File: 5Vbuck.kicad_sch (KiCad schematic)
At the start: 0 parts

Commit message: jobbing med 5V og 12V
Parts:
- added C_BST1, C_Vin1: 0.1u, symbol Device:C
- added C_C4: 4.7n, symbol Device:C
- added C_C5: 100p, symbol Device:C
- added C_C6: 1n, symbol Device:C
- added C_ss1: 12.5n, symbol Device:C
- added R_BST1, R_Vin1: 2.2, symbol Device:R
- added R_C3: 8.06k, symbol Device:R
- added R_C4, R_UV4: 100k, symbol Device:R
- added R_FB1: 52.5k, symbol Device:R
- added R_FB2: 10k, symbol Device:R
- added R_RT1: 24.9k, symbol Device:R
- added R_UV3: 9.31k, symbol Device:R
- added U3: LM5146RGYR, LM5146RGYR:IC_LM5146RGYR, symbol LM5146RGYR:LM5146RGYR
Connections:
- new net: C_C4.1, R_C3.1
- new net: C_C5.2, C_C6.1, R_C3.2, R_C4.2, R_FB2.1
- new net: C_Vin1.2, R_UV4.2, R_Vin1.1, U3.20 (VIN)
- new net: C_C4.2, C_C5.1
- new net: R_BST1.1, U3.17 (BST)
- new net: C_BST1.1, R_BST1.2
- new net: C_BST1.2, U3.19 (SW)
- new net: R_UV3.2, R_UV4.1, U3.1 (EN/UVLO)
- new net: C_ss1.2, U3.3 (SS/TRK)
- new net: U3.16 (NC), U3.9 (NC)
- new net: R_RT1.2, U3.2 (RT)
- new net: R_C4.1, R_FB1.2
- new net: C_C6.2, R_FB1.1
- new net 5VSYNC_In: U3.8 (SYNCIN)
- new net 5VSYNC_Out: U3.7 (SYNCOUT)
- new net 5V_PGOOD: U3.10 (PGOOD)
- new net 5V_Vin: R_Vin1.2
- new net EP: U3.15 (EP), U3.21 (EP)
- new net GND: C_Vin1.1, C_ss1.1, R_FB2.2, R_RT1.1, R_UV3.1, U3.11 (ILIM), U3.6 (AGND)
- no-connect marks 0 -> 1

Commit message: navn på alle komp i 5V
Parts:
- removed C_BST1, C_Vin1: 0.1u, symbol Device:C
- removed C_C4: 4.7n, symbol Device:C
- removed C_C5: 100p, symbol Device:C
- removed C_C6: 1n, symbol Device:C
- removed C_ss1: 12.5n, symbol Device:C
- removed R_BST1, R_Vin1: 2.2, symbol Device:R
- removed R_C3: 8.06k, symbol Device:R
- removed R_C4, R_UV4: 100k, symbol Device:R
- removed R_FB1: 52.5k, symbol Device:R
- removed R_FB2: 10k, symbol Device:R
- removed R_RT1: 24.9k, symbol Device:R
- removed R_UV3: 9.31k, symbol Device:R
- added C401, C404: 0.1u, symbol Device:C
- added C402: 2.2u, symbol Device:C
- added C403: 47nF, symbol Device:C
- added C405: 10p, symbol Device:C
- added C406: 4.7n, symbol Device:C
- added C407: 100p, symbol Device:C
- added C408: 1n, symbol Device:C
- added C409, C410, C411, C412, C413: 2.2 u, symbol Device:C
- added C414, C415, C416, C417, C418: 22u, symbol Device:C
- added L401: L, Package_SO:SSOP-16_3.9x4.9mm_P0.635mm, symbol Device:L
- added Q3, Q4: NMOS, Package_DFN_QFN:Nordic_AQFN-94-1EP_7x7mm_P0.4mm, symbol Simulation_SPICE:NMOS
- added R401: 9.31k, symbol Device:R
- added R402, R409: 100k, symbol Device:R
- added R403, R405: 2.2, symbol Device:R
- added R406: 24.9 k, symbol Device:R
- added R407: 619, symbol Device:R
- added R408: 8.06k, symbol Device:R
- added R410: 21k, symbol Device:R
- added R411: 1.5k, symbol Device:R
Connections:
- net GND: now also U3.12 (PGND), C401.1, C402.2, C403.1, C405.2, C413.2, C418.2, Q4.3 (S), R401.1, R406.1, R411.2; no longer U3.11 (ILIM)
- net at U3.20 (VIN): now also C401.2, R402.2, R403.1
- net at U3.17 (BST): now also R405.1
- net at U3.19 (SW): now also C404.2, L401.1, Q3.3 (S), Q4.1 (D), R407.2
- net at U3.1 (EN/UVLO): now also R401.2, R402.1
- net at U3.3 (SS/TRK): now also C403.2
- net at U3.13 (LO): now also Q4.2 (G)
- net at U3.14 (VCC): now also C402.1
- net at U3.18 (HO): now also Q3.2 (G)
- net at U3.2 (RT): now also R406.2
- net Comp: now reaches U3.4 (COMP)
- net Comp: now also C406.2, C407.1
- net FB: now reaches U3.5 (FB)
- net FB: now also C407.2, C408.1, R408.2, R409.2, R411.1
- net 5VSYNC_In renamed 12VSYNC_In
- net 5VSYNC_Out renamed 12VSYNC_Out
- net 5V_PGOOD renamed 12V_PGOOD
- new net: C411.2, C412.1
- new net: C412.2, C413.1
- new net: C409.2, C410.1
- new net: C416.2, C417.1
- new net: C417.2, C418.1
- new net: C405.1, R407.1, U3.11 (ILIM)
- new net: C414.2, C415.1
- new net: C404.1, R405.2
- new net: C408.2, R410.1
- new net: C406.1, R408.1
- new net: C415.2, C416.1
- new net: C410.2, C411.1
- new net 12VV_out: C414.1, L401.2, R409.1, R410.2
- new net 12V_Vin: C409.1, Q3.1 (D), R403.2

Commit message: endring av kondensatorer
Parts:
- added R411: 20k, symbol Device:R
- C403: value 47nF -> 12.5nF
- C405: value 10p -> 47p
- C406: value 4.7n -> 2.3n
- C407: value 100p -> 22p
- C408: value 1n -> 820p
- L401: value L -> 15u
- R401: value 9.31k -> 14.3k
- R402: value 100k -> 200k
- R406: renamed from R407; value 619 -> 134
- R407: renamed from R408; value 8.06k -> 35.7k
- R408: renamed from R409; value 100k -> 52.5k; Field5 R_C2 -> R_FB1
- R409: renamed from R410; value 21k -> 100k; Field5 R_FB1 -> R_C2
- R410: renamed from R411; value 1.5k -> 10k; Field5 R_FB1 -> R_FB2
- renumbered R405 to R404, R406 to R405
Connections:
- net 12VV_out is gone; now on net 5V_Vout: C414.1, L401.2, R408.1, R409.2
- net 12V_Vin is gone; now on net 5V_Vin: C409.1, Q3.1 (D), R403.2
- net GND: now also C409.2, C410.2, C411.2, C412.2, C414.2, C415.2, C416.2, C417.2
- net 5V_Vin: now reaches C412.1
- net 5V_Vin: now also C410.1, C411.1, C413.1; no longer C411.2
- net V_cc: now reaches C402.1, U3.14 (VCC)
- net V_cc: now also R411.1
- net 5V_Vout: now reaches C417.1
- net 5V_Vout: now also C415.1, C416.1, C418.1; no longer C416.2
- net at C405.1, R406.1, U3.11 (ILIM): now also R411.2
- net 12VSYNC_In renamed 5VSYNC_In
- net 12VSYNC_Out renamed 5VSYNC_Out
- net 12V_PGOOD renamed 5V_PGOOD
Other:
- moved on the sheet: C406, C407, C408, C409, C410, C411, C412, C413, C414, C415, C416, C417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

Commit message: komp til 5V
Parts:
- C405: value 47p -> 39p
- C406: value 2.3n -> 12n
- C407: value 22p -> 120p
- C408: value 820p -> 4.7n
- R401: value 14.3k -> 12.7k
- R406: value 134 -> 137
- R407: value 35.7k -> 6.8k
- R408: value 52.5k -> 10k
- R409: value 100k -> 350
- R410: value 10k -> 1.91k
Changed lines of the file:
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@@
 			)
 		)
-		(property "Value" "134"
+		(property "Value" "137"
 			(at 124.46 123.19 90)
 			(show_name no)
@@
 			)
 		)
-		(property "Value" "14.3k"
+		(property "Value" "12.7k"
 			(at 66.04 62.23 90)
 			(show_name no)
@@
 			)
 		)
-		(property "Value" "10k"
+		(property "Value" "1.91k"
 			(at 176.53 139.6999 0)
 			(show_name no)
@@
 			)
 		)
-		(property "Value" "22p"
+		(property "Value" "120p"
 			(at 163.83 133.858 90)
 			(show_name no)
@@
 			)
 		)
-		(property "Value" "820p"
+		(property "Value" "4.7n"
 			(at 186.69 121.9199 0)
 			(show_name no)
@@
 			)
 		)
-		(property "Value" "2.3n"
+		(property "Value" "12n"
 			(at 160.02 115.57 90)
 			(show_name no)
@@
 			)
 		)
-		(property "Value" "52.5k"
+		(property "Value" "10k"
 			(at 176.53 116.8399 0)
 			(show_name no)
@@
 			)
 		)
-		(property "Value" "35.7k"
+		(property "Value" "6.8k"
 			(at 167.64 116.84 90)
 			(show_name no)
@@
 			)
 		)
-		(property "Value" "47p"
+		(property "Value" "39p"
 			(at 120.65 133.3499 0)
 			(show_name no)
@@
 			)
 		)
-		(property "Value" "100k"
+		(property "Value" "350"
 			(at 185.42 114.2999 0)
 			(show_name no)

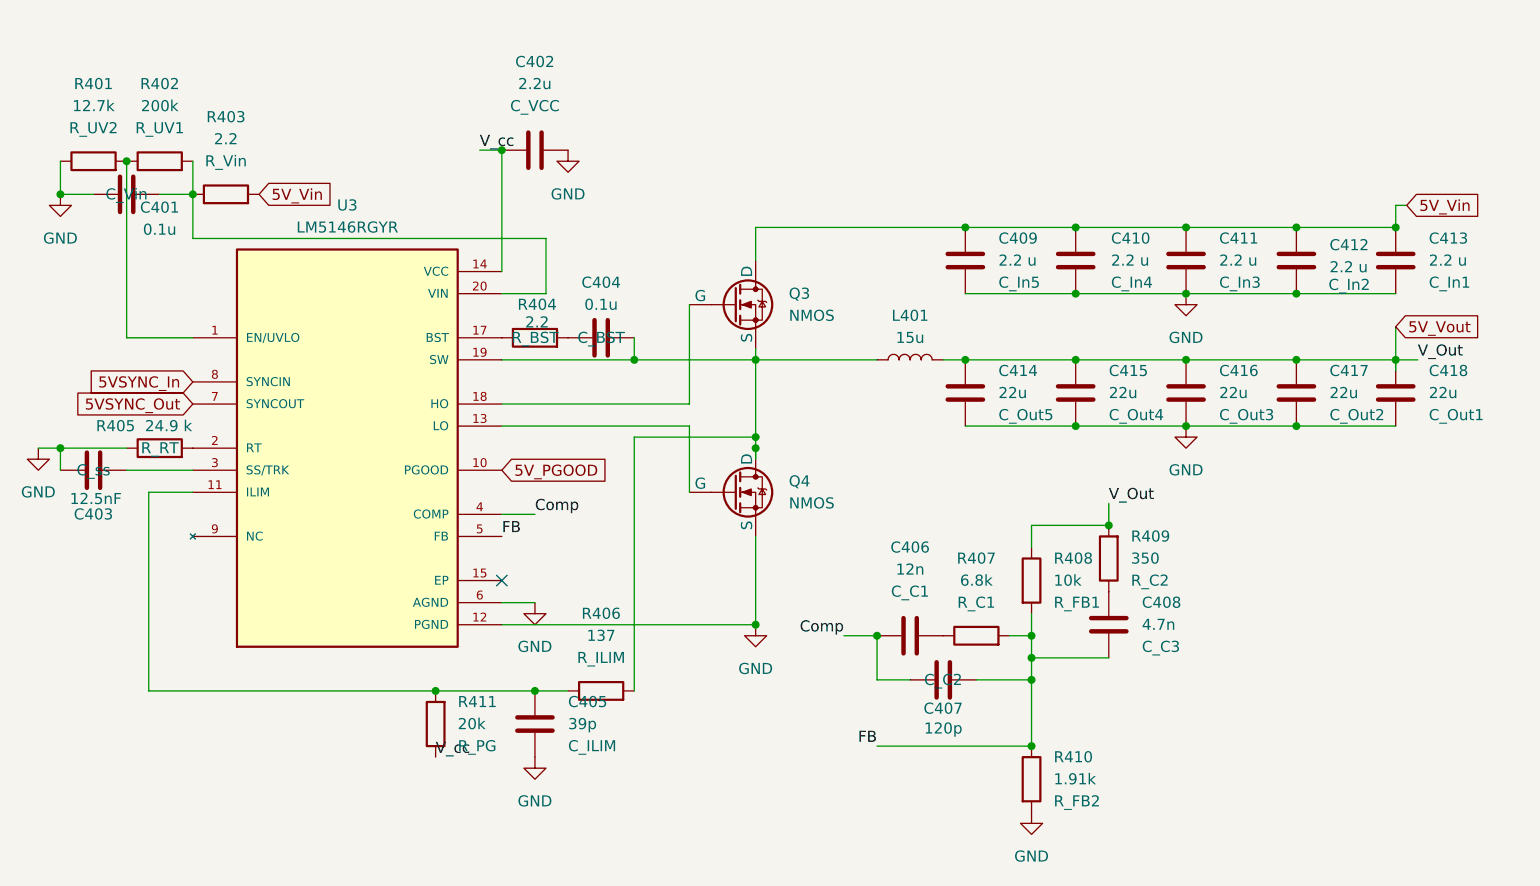
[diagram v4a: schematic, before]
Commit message: alle komponenter har fått rett navn
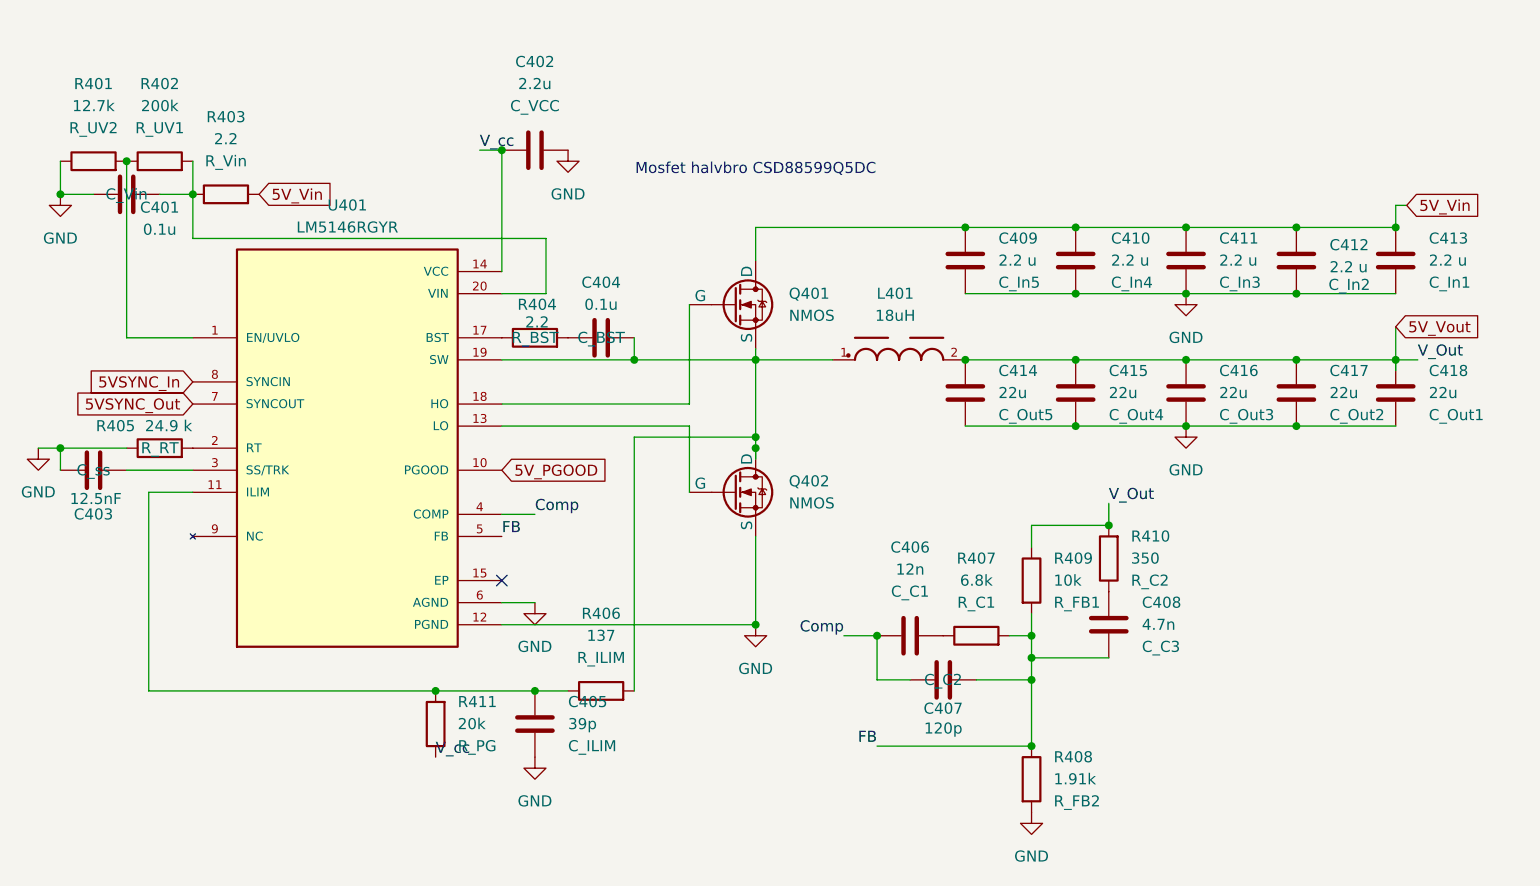
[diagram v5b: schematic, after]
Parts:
- removed L401: 15u, Package_SO:SSOP-16_3.9x4.9mm_P0.635mm, symbol Device:L
- added L401: 18uH, WE-PD_1245:WE-PD_1245, symbol Halfdan:WE-PD_1245
- renumbered Q3 to Q401, Q4 to Q402, R410 to R408, R408 to R409, R409 to R410, U3 to U401
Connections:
- net 5V_Vout: now also L401.2
- net at C404.2, Q401.3 (S), Q402.1 (D)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: now also L401.1
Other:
- note added: "Mosfet halvbro CSD88599Q5DC"
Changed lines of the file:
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@@
 	(generator_version "10.0")
 	(paper "A4")
+	(text "Mosfet halvbro CSD88599Q5DC "
+		(exclude_from_sim no)
+		(at 142.24 69.596 0)
+		(effects
+			(font
+				(size 1.27 1.27)
+			)
+		)
+	)
 	(junction
 		(at 166.37 76.2)
@@
 	)
 	(junction
+		(at 166.37 91.44)
+		(diameter 0)
+		(color 0 0 0 0)
+	)
+	(junction
 		(at 179.07 76.2)
 		(diameter 0)
@@
 	)
 	(junction
-		(at 166.37 91.44)
-		(diameter 0)
-		(color 0 0 0 0)
-	)
-	(junction
 		(at 142.24 101.6)
 		(diameter 0)
@@
 	(wire
 		(pts
-			(xy 142.24 91.44) (xy 156.21 91.44)
-		)
-		(stroke
-			(width 0)
-			(type default)
-		)
-	)
-	(wire
-		(pts
 			(xy 134.62 96.52) (xy 134.62 85.09)
 		)
@@
 	(wire
 		(pts
-			(xy 77.47 72.39) (xy 77.47 77.47)
+			(xy 142.24 91.44) (xy 151.13 91.44)
 		)
 		(stroke
@@
 	(wire
 		(pts
-			(xy 163.83 91.44) (xy 166.37 91.44)
+			(xy 77.47 72.39) (xy 77.47 77.47)
 		)
 		(stroke
@@
 		(dnp no)
 		(fields_autoplaced yes)
-		(property "Reference" "U3"
+		(property "Reference" "U401"
 			(at 95.25 73.66 0)
 			(show_name no)
@@
 			(project "ProteusPowerManagment"
 				(path "/c24111dd-5300-4143-a3c3-2d963194a3cb/ff489ca0-c022-46f0-934f-be95c81d38e4"
-					(reference "U3")
+					(reference "U401")
 					(unit 1)
 				)
@@
 		(dnp no)
 		(fields_autoplaced yes)
-		(property "Reference" "R410"
+		(property "Reference" "R408"
 			(at 176.53 137.1599 0)
 			(show_name no)
@@
 			(project "ProteusPowerManagment"
 				(path "/c24111dd-5300-4143-a3c3-2d963194a3cb/ff489ca0-c022-46f0-934f-be95c81d38e4"
-					(reference "R410")
+					(reference "R408")
 					(unit 1)
 				)
@@
 		(dnp no)
 		(fields_autoplaced yes)
-		(property "Reference" "Q3"
+		(property "Reference" "Q401"
 			(at 146.05 83.8199 0)
 			(show_name no)
@@
 			(project "ProteusPowerManagment"
 				(path "/c24111dd-5300-4143-a3c3-2d963194a3cb/ff489ca0-c022-46f0-934f-be95c81d38e4"
-					(reference "Q3")
+					(reference "Q401")
 					(unit 1)
 				)
@@
 		(dnp no)
 		(fields_autoplaced yes)
-		(property "Reference" "Q4"
+		(property "Reference" "Q402"
 			(at 146.05 105.4099 0)
 			(show_name no)
@@
 			(project "ProteusPowerManagment"
 				(path "/c24111dd-5300-4143-a3c3-2d963194a3cb/ff489ca0-c022-46f0-934f-be95c81d38e4"
-					(reference "Q4")
+					(reference "Q402")
 					(unit 1)
 				)
@@
 	)
 	(symbol
-		(lib_id "Device:L")
-		(at 160.02 91.44 90)
-		(unit 1)
-		(body_style 1)
-		(exclude_from_sim no)
-		(in_bom yes)
-		(on_board yes)
-		(in_pos_files yes)
-		(dnp no)
-		(fields_autoplaced yes)
-		(property "Reference" "L401"
-			(at 160.02 86.36 90)
-			(show_name no)
-			(do_not_autoplace no)
-			(effects
-				(font
-					(size 1.27 1.27)
-				)
-			)
-		)
-		(property "Value" "15u"
-			(at 160.02 88.9 90)
-			(show_name no)
-			(do_not_autoplace no)
-			(effects
-				(font
-					(size 1.27 1.27)
-				)
-			)
-		)
-		(property "Footprint" "Package_SO:SSOP-16_3.9x4.9mm_P0.635mm"
-			(at 160.02 91.44 0)
-			(hide yes)
-			(show_name no)
-			(do_not_autoplace no)
-			(effects
-				(font
-					(size 1.27 1.27)
-				)
-			)
-		)
-		(property "Datasheet" ""
-			(at 160.02 91.44 0)
-			(hide yes)
-			(show_name no)
-			(do_not_autoplace no)
-			(effects
-				(font
-					(size 1.27 1.27)
-				)
-			)
-		)
-		(property "Description" "Inductor"
-			(at 160.02 91.44 0)
-			(hide yes)
-			(show_name no)
-			(do_not_autoplace no)
-			(effects
-				(font
-					(size 1.27 1.27)
-				)
-			)
-		)
-		(pin "1"
-		)
-		(pin "2"
-		)
-		(instances
-			(project "ProteusPowerManagment"
-				(path "/c24111dd-5300-4143-a3c3-2d963194a3cb/ff489ca0-c022-46f0-934f-be95c81d38e4"
-					(reference "L401")
-					(unit 1)
-				)
-			)
-		)
-	)
-	(symbol
 		(lib_id "power:GND")
 		(at 116.84 119.38 0)
@@
 		(dnp no)
 		(fields_autoplaced yes)
-		(property "Reference" "R408"
+		(property "Reference" "R409"
 			(at 176.53 114.2999 0)
 			(show_name no)
@@
 			(project "ProteusPowerManagment"
 				(path "/c24111dd-5300-4143-a3c3-2d963194a3cb/ff489ca0-c022-46f0-934f-be95c81d38e4"
-					(reference "R408")
+					(reference "R409")
 					(unit 1)
 				)
@@
 	)
 	(symbol
+		(lib_id "Halfdan:WE-PD_1245")
+		(at 158.75 91.44 0)
+		(unit 1)
+		(body_style 1)
+		(exclude_from_sim no)
+		(in_bom yes)
+		(on_board yes)
+		(in_pos_files yes)
+		(dnp no)
+		(fields_autoplaced yes)
+		(property "Reference" "L401"
+			(at 158.3055 83.82 0)
+			(show_name no)
+			(do_not_autoplace no)
+			(effects
+				(font
+					(size 1.27 1.27)
+				)
+			)
+		)
+		(property "Value" "18uH"
+			(at 158.3055 86.36 0)
+			(show_name no)
+			(do_not_autoplace no)
+			(effects
+				(font
+					(size 1.27 1.27)
+				)
+			)
+		)
+		(property "Footprint" "WE-PD_1245:WE-PD_1245"
+			(at 158.75 91.44 0)
+			(hide yes)
+			(show_name no)
+			(do_not_autoplace no)
+			(effects
+				(font
+					(size 1.27 1.27)
+				)
+				(justify bottom)
+			)
+		)
+		(property "Datasheet" ""
+			(at 158.75 91.44 0)
+			(hide yes)
+			(show_name no)
+			(do_not_autoplace no)
+			(effects
+				(font
+					(size 1.27 1.27)
+				)
+			)
+		)
+		(property "Description" ""
+			(at 158.75 91.44 0)
+			(hide yes)
+			(show_name no)
+			(do_not_autoplace no)
+			(effects
+				(font
+					(size 1.27 1.27)
+				)
+			)
+		)
+		(pin "2"
+		)
+		(pin "1"
+		)
+		(instances
+			(project "ProteusPowerManagment"
+				(path "/c24111dd-5300-4143-a3c3-2d963194a3cb/ff489ca0-c022-46f0-934f-be95c81d38e4"
+					(reference "L401")
+					(unit 1)
+				)
+			)
+		)
+	)
+	(symbol
 		(lib_id "power:GND")
 		(at 62.23 72.39 0)
@@
 		(dnp no)
 		(fields_autoplaced yes)
-		(property "Reference" "R409"
+		(property "Reference" "R410"
 			(at 185.42 111.7599 0)
 			(show_name no)
@@
 			(project "ProteusPowerManagment"
 				(path "/c24111dd-5300-4143-a3c3-2d963194a3cb/ff489ca0-c022-46f0-934f-be95c81d38e4"
-					(reference "R409")
+					(reference "R410")
 					(unit 1)
 				)

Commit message: rettet opp på komp
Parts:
- C405: value 39p -> 33p
- R406: value 137 -> 178
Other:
- note added: "Mosfet samme kapsling NVMFD5C674NL"
- note removed: "Mosfet halvbro CSD88599Q5DC"
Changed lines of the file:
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@@
 	(generator_version "10.0")
 	(paper "A4")
-	(text "Mosfet halvbro CSD88599Q5DC "
+	(text "Mosfet  samme kapsling NVMFD5C674NL"
 		(exclude_from_sim no)
 		(at 142.24 69.596 0)
@@
 			)
 		)
-		(property "Value" "137"
+		(property "Value" "178"
 			(at 124.46 123.19 90)
 			(show_name no)
@@
 			)
 		)
-		(property "Value" "39p"
+		(property "Value" "33p"
 			(at 120.65 133.3499 0)
 			(show_name no)

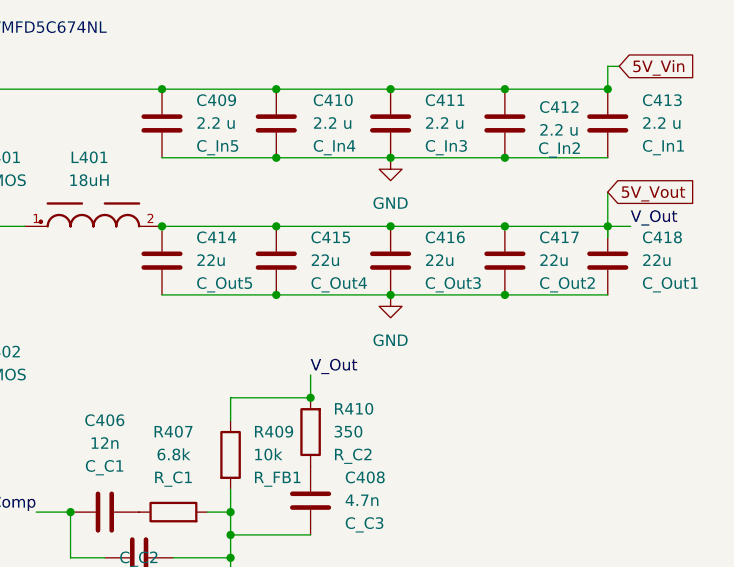
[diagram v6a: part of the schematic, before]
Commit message: måtte endre på footprints i 5v da de ikke var lik BOM
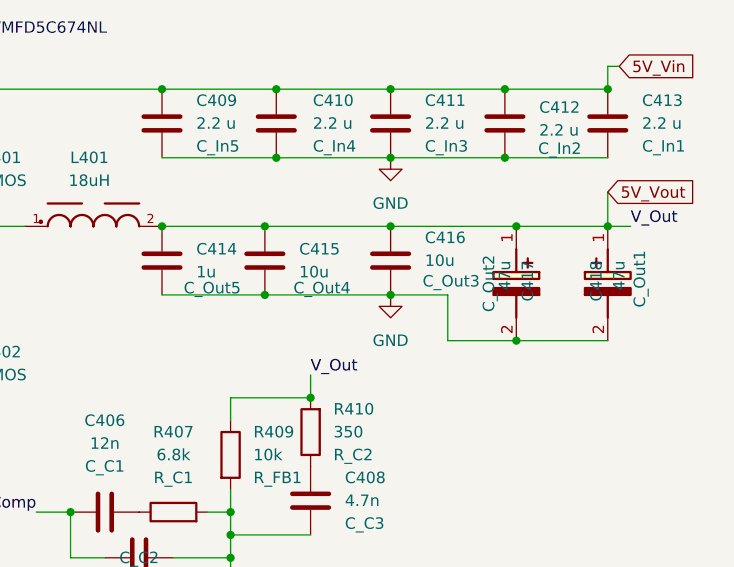
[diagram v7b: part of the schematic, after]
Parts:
- removed C417, C418: 22u, symbol Device:C
- added C417, C418: 47u, CAPAE830X1000N, symbol Halfdan:APA0809470M050R
- C409, C410, C411, C412, C413: footprint (none) -> Capacitor_SMD:C_1210_3225Metric
- C414: value 22u -> 1u; footprint (none) -> Capacitor_SMD:C_0805_2012Metric; Field6 (none) -> GMK212B7105MG-T
- C415, C416: value 22u -> 10u; footprint (none) -> Capacitor_SMD:C_1206_3216Metric; Field6 (none) -> MSASG31LAB7106MTNB25
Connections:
- net 5V_Vout: now also C417.1 (+), C418.1 (+)
- net GND: now also C417.2 (-), C418.2 (-)
